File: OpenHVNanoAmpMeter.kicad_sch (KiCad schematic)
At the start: 2 parts, among them J1 Conn_Coaxial, J2 Conn_Coaxial

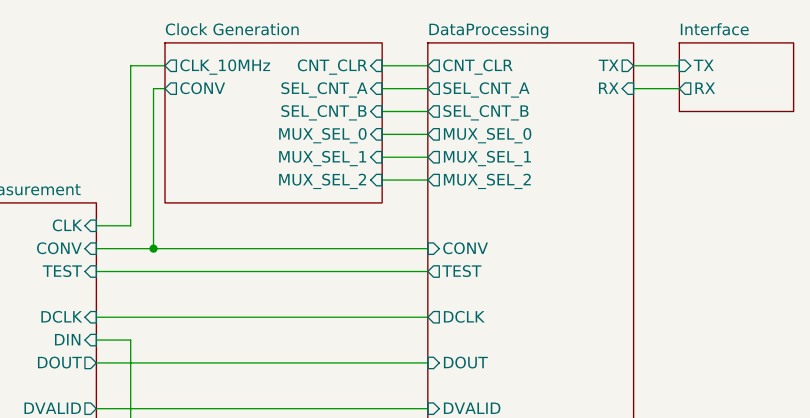
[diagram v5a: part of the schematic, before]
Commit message: changed setting of clock divider to I2C
reduces pin load on uC, thus frees pins for usage with other functions.
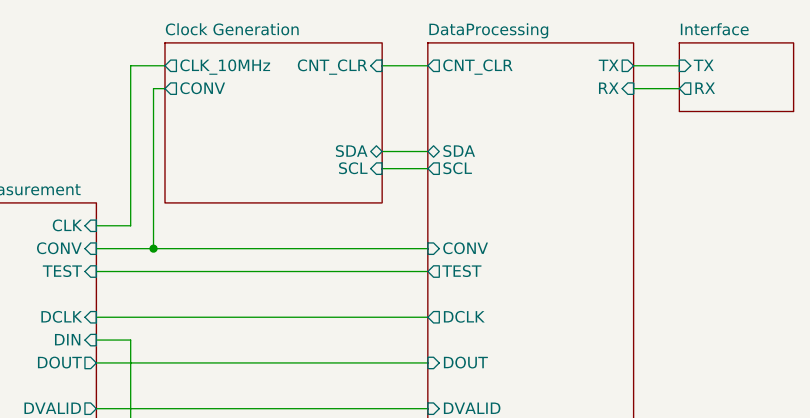
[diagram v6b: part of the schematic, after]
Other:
- sheet Clock Generation ports: added SCL, SDA; removed MUX_SEL_0, MUX_SEL_1, MUX_SEL_2, SEL_CNT_A, SEL_CNT_B
- sheet DataProcessing ports: added SCL, SDA; removed MUX_SEL_0, MUX_SEL_1, MUX_SEL_2, SEL_CNT_A, SEL_CNT_B

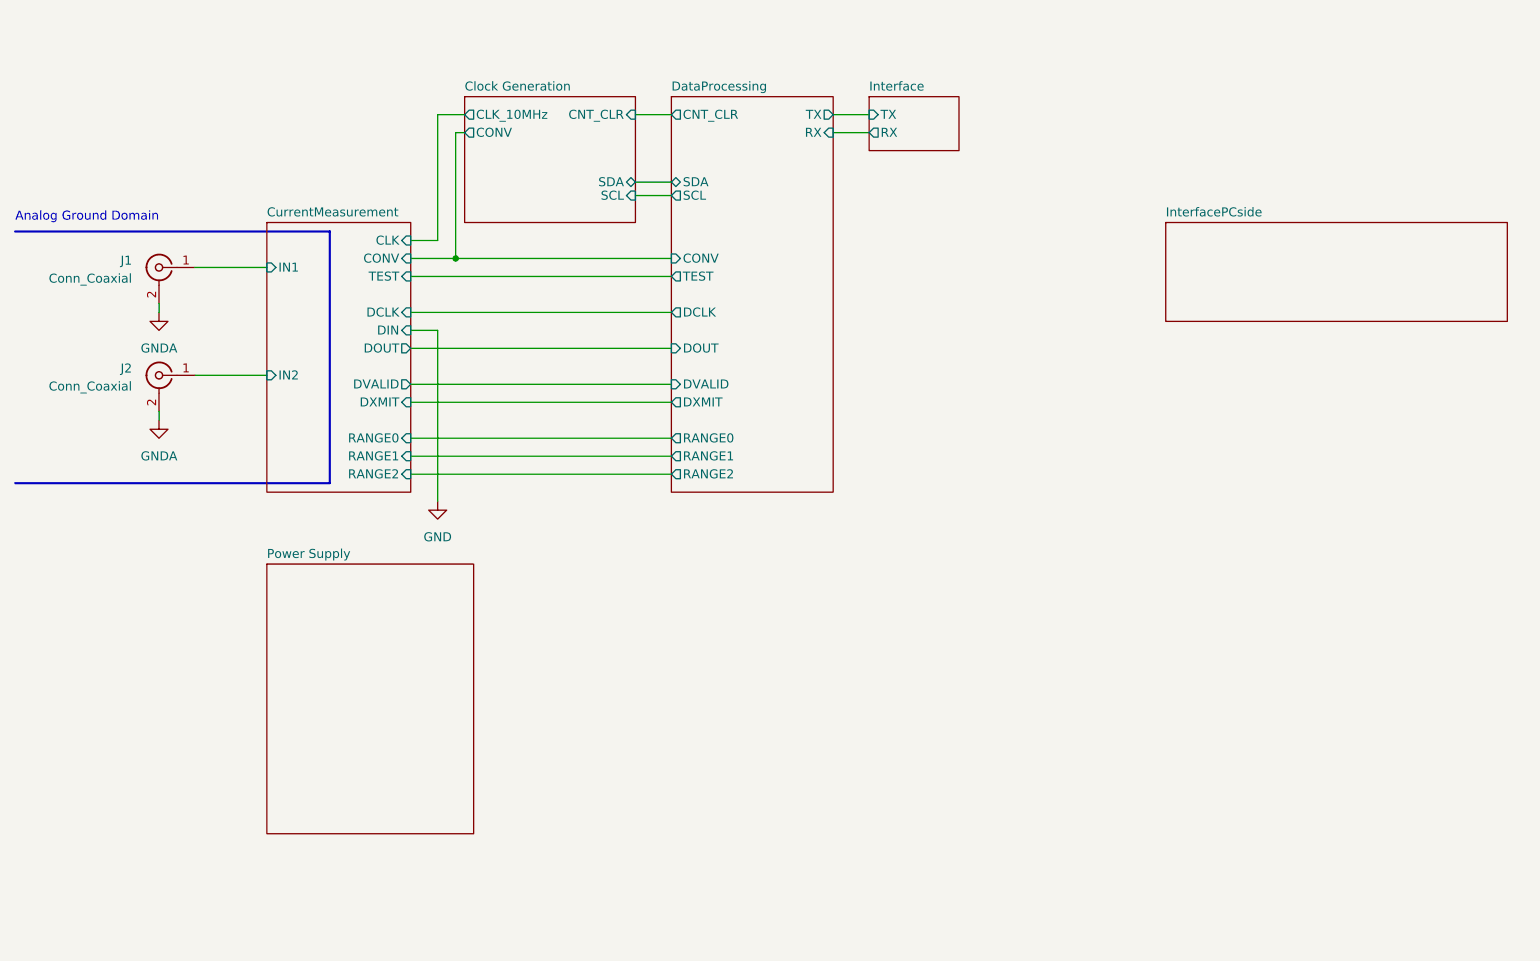
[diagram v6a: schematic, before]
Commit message: added mounting holes and renamed TX & RX to LWL*
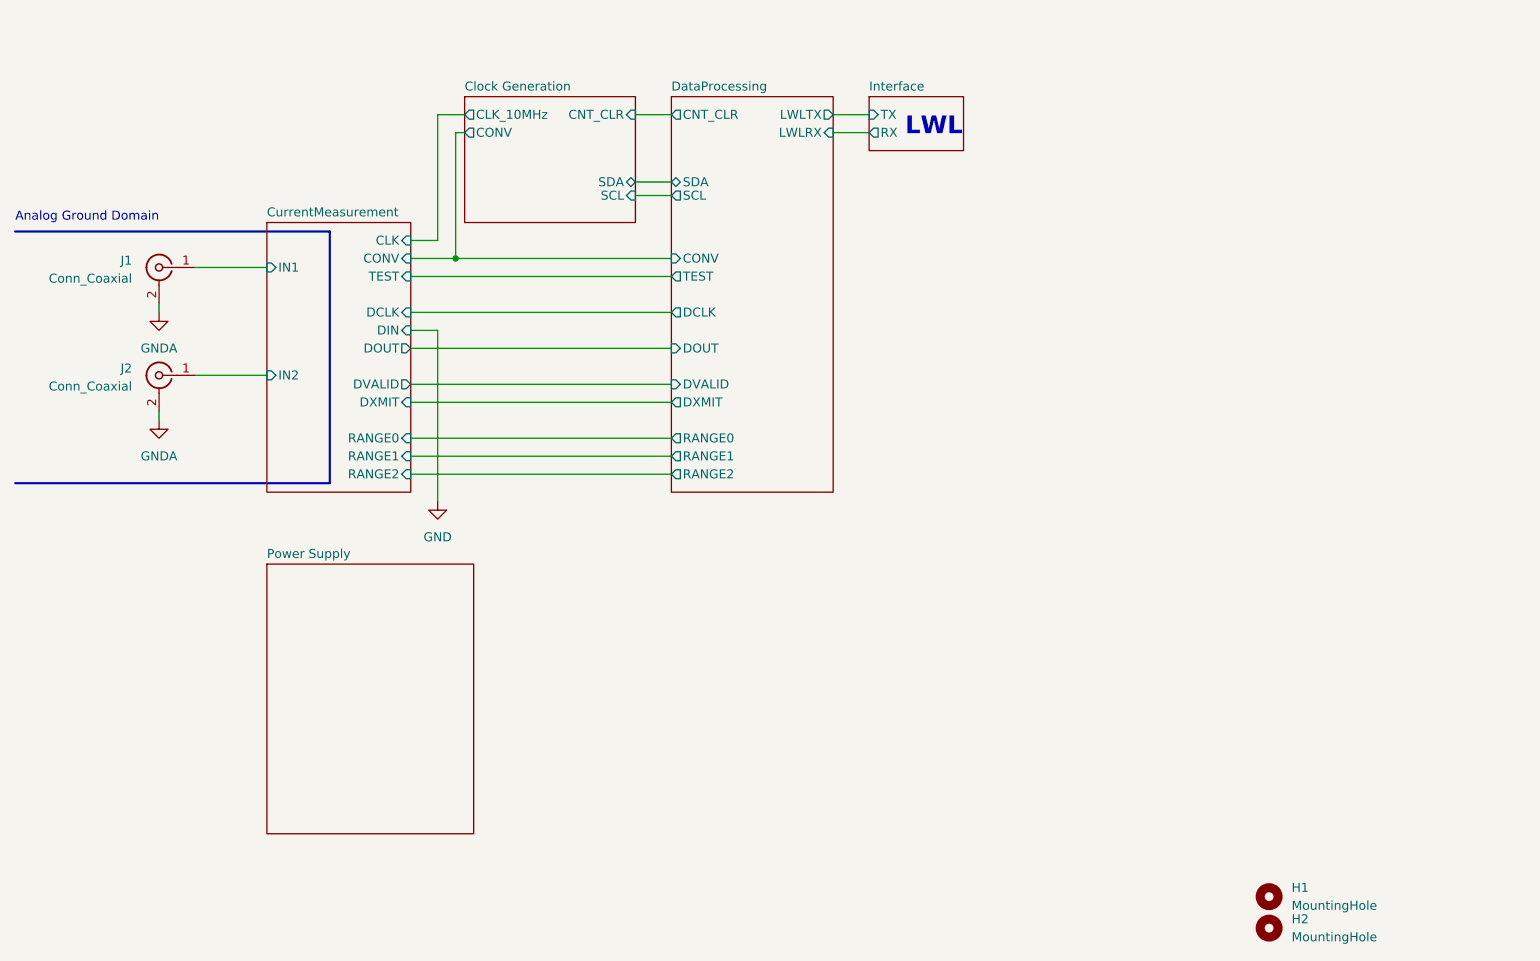
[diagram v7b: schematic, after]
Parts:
- added H1, H2: MountingHole, MountingHole:MountingHole_3.2mm_M3_DIN965, symbol Mechanical:MountingHole
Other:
- removed sheet InterfacePCside
- sheet DataProcessing ports: added LWLRX, LWLTX; removed RX, TX
- note added: "LWL"
